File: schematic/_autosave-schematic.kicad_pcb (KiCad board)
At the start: 2 copper layers, 1 part

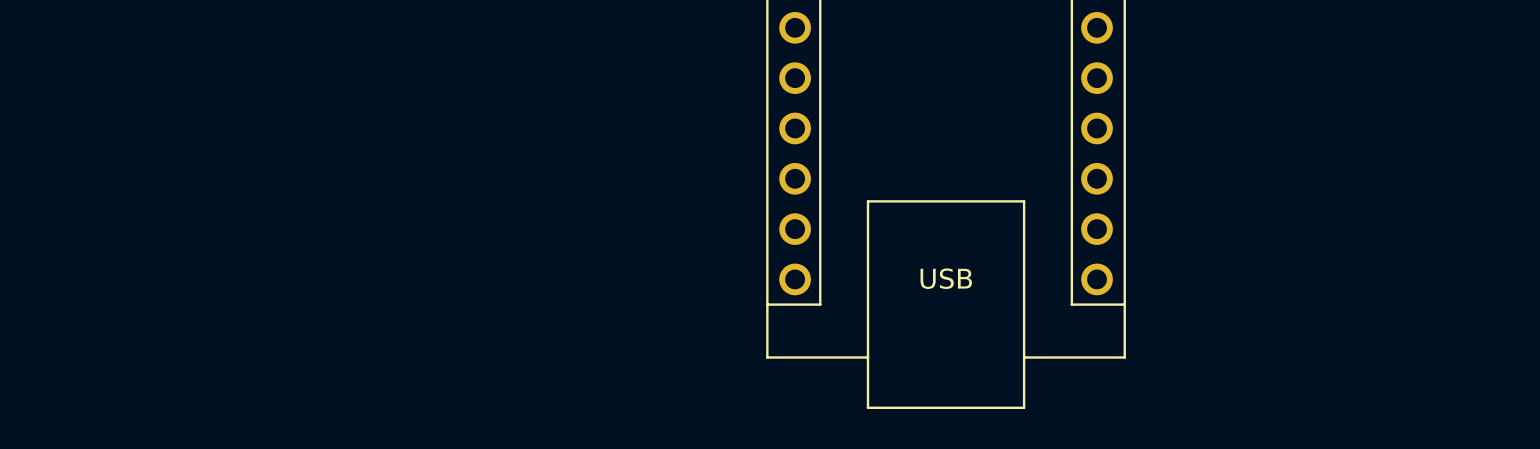
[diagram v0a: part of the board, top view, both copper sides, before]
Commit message: I think we need to give up on the branches...it's becoming really obvious that it's not working and I'm not really using gitHub for version control (that or it just hasn't gotten bad enough to need the version control, one or the other)
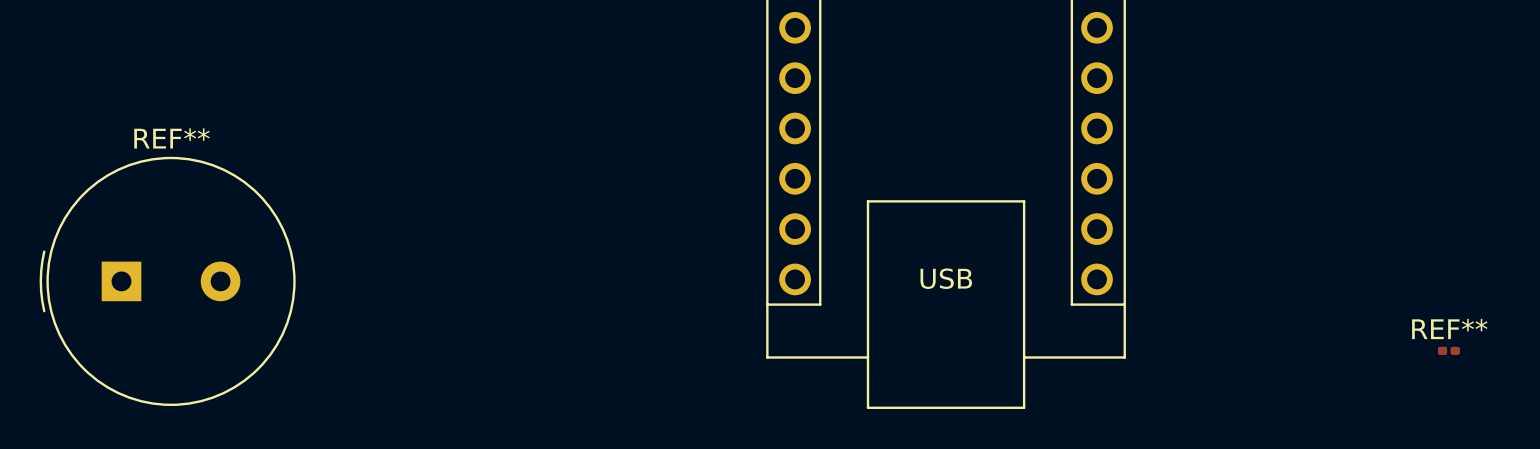
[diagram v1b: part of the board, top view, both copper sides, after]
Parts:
- added REF**: C_0201_0603Metric, Capacitor_SMD:C_0201_0603Metric, F.Cu at (218.5, 94.0)
- added REF**: Buzzer_TDK_PS1240P02BT_D12.2mm_H6.5mm, Buzzer_Beeper:Buzzer_TDK_PS1240P02BT_D12.2mm_H6.5mm, F.Cu at (151.5, 90.5)

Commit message: arduino firmware
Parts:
- moved A1 3.23 mm to (186.3, 58.0)
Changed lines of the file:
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@@
 	(footprint "Module:Arduino_Nano"
 		(layer "F.Cu")
-		(at 185.5 54.84)
+		(at 186.26 57.98)
 		(descr "Arduino Nano, http://www.mouser.com/pdfdocs/Gravitech_Arduino_Nano3_0.pdf")
 		(tags "Arduino Nano")
@@
 		)
 	)
+	(gr_rect
+		(start 52 39.5)
+		(end 111.5 161)
+		(stroke
+			(width 0.2)
+			(type default)
+		)
+		(fill no)
+		(layer "F.Cu")
+	)
 	(embedded_fonts no)
